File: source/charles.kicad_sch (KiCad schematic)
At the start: 35 parts, among them J1 HRO-TYPE-C-31-M-13C, J2 Tag-Connect_Plug_of_nails_6pin, J3 Solder Battery, J4 JST ACH, Q1 AO3401A, Q2 Q_NMOS_DGS, SW38 Reset Switch, SW39 Soft Off, U1 MS88SF3, U2 USBLC6-2P6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

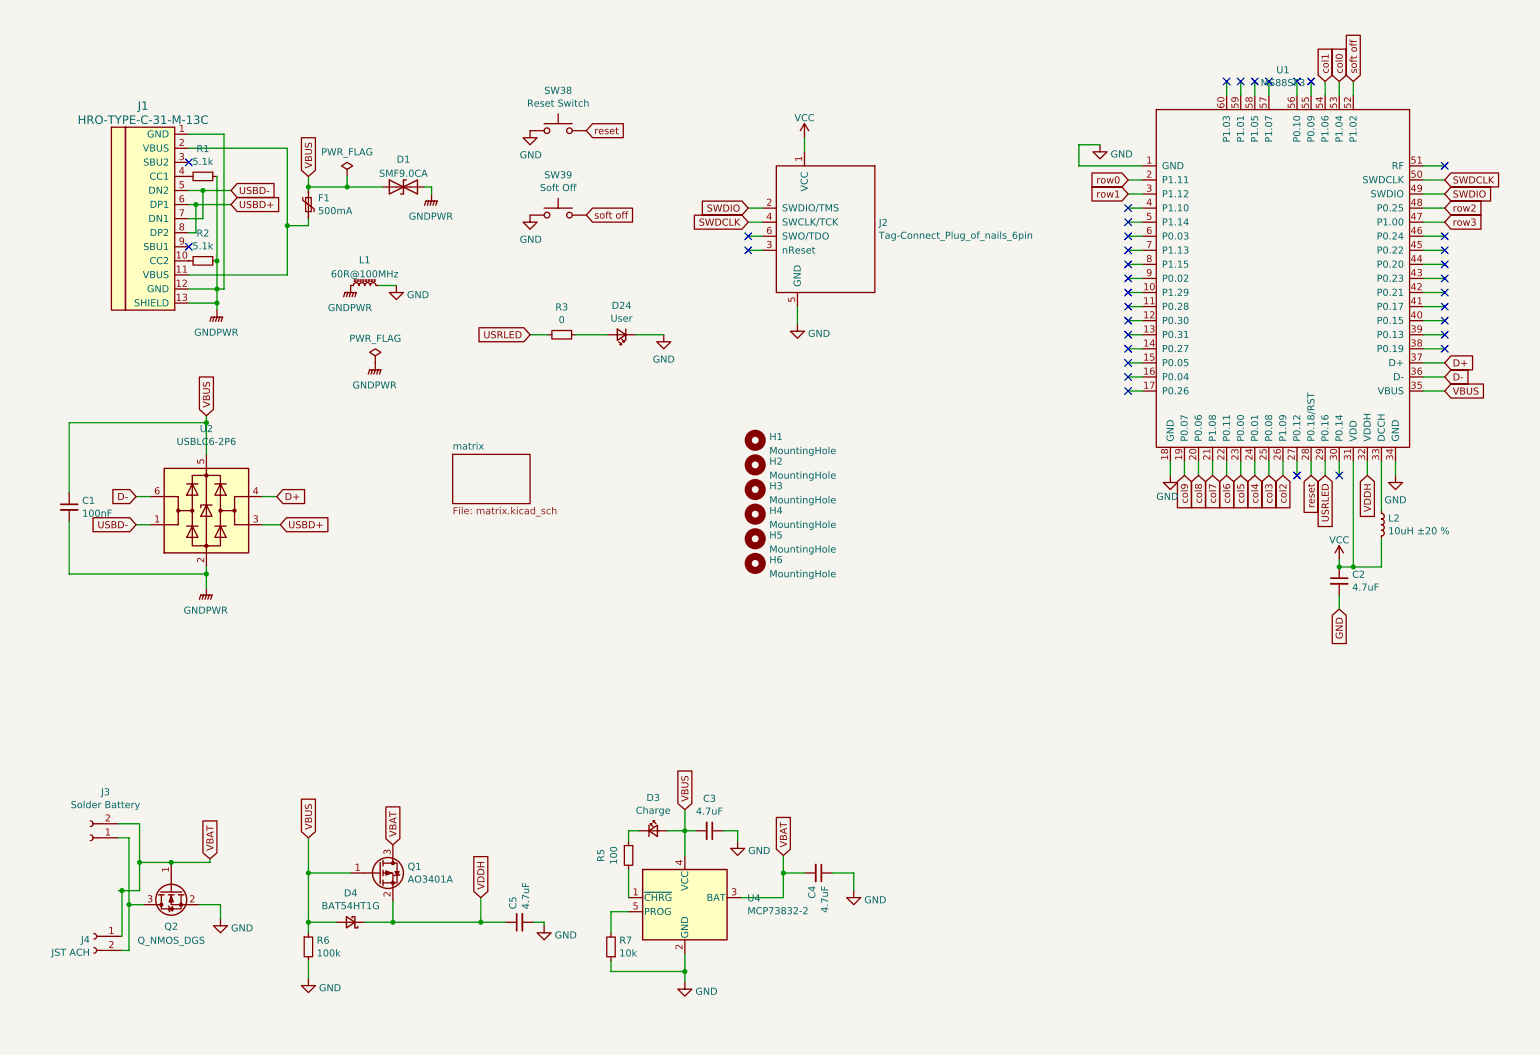
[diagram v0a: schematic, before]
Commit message: added non-jtag flash interface, zmk/osh silk, rearranging tracks
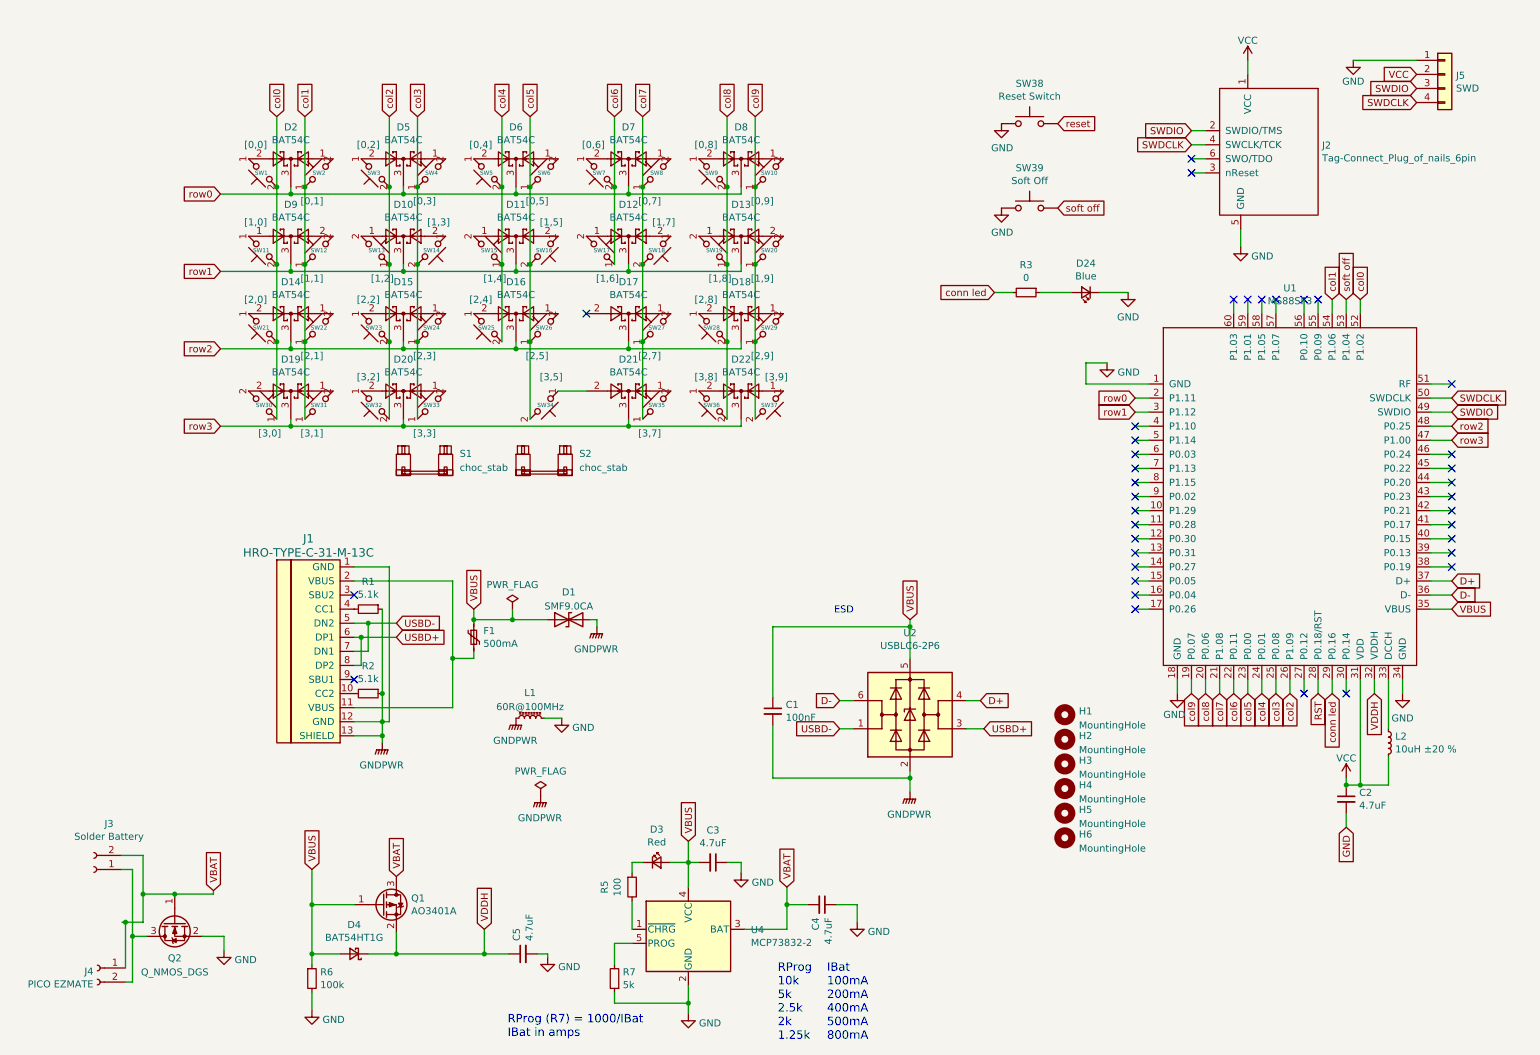
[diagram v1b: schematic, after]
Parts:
- added D10, D11, D12, D13, D14, D15, D16, D17, D18, D19, D2, D20, D21, D22, D5, D6, D7, D8, D9: BAT54C, Package_TO_SOT_SMD:SOT-23, symbol Diode:BAT54C
- added J5: SWD, Connector_PinHeader_2.54mm:PinHeader_1x04_P2.54mm_Vertical, symbol Connector_Generic:Conn_01x04
- added S1, S2: choc_stab, PCM_marbastlib-xp-choc:STAB_choc_2u, symbol PCM_marbastlib-choc:choc_stab
- added SW1: [0,0], chaz:choc-1u-millmax, symbol Switch:SW_Push_45deg
- added SW10: [0,9], chaz:choc-1u-millmax, symbol Switch:SW_Push_45deg
- added SW11: [1,0], chaz:choc-1u-millmax, symbol Switch:SW_Push_45deg
- added SW12: [1,1], chaz:choc-1u-millmax, symbol Switch:SW_Push_45deg
- added SW13: [1,2], chaz:choc-1u-millmax, symbol Switch:SW_Push_45deg
- added SW14: [1,3], chaz:choc-1u-millmax, symbol Switch:SW_Push_45deg
- added SW15: [1,4], chaz:choc-1u-millmax, symbol Switch:SW_Push_45deg
- added SW16: [1,5], chaz:choc-1u-millmax, symbol Switch:SW_Push_45deg
- added SW17: [1,6], chaz:choc-1u-millmax, symbol Switch:SW_Push_45deg
- added SW18: [1,7], chaz:choc-1u-millmax, symbol Switch:SW_Push_45deg
- added SW19: [1,8], chaz:choc-1u-millmax, symbol Switch:SW_Push_45deg
- added SW2: [0,1], chaz:choc-1u-millmax, symbol Switch:SW_Push_45deg
- added SW20: [1,9], chaz:choc-1u-millmax, symbol Switch:SW_Push_45deg
- added SW21: [2,0], chaz:choc-1u-millmax, symbol Switch:SW_Push_45deg
- added SW22: [2,1], chaz:choc-1u-millmax, symbol Switch:SW_Push_45deg
- added SW23: [2,2], chaz:choc-1u-millmax, symbol Switch:SW_Push_45deg
- added SW24: [2,3], chaz:choc-1u-millmax, symbol Switch:SW_Push_45deg
- added SW25: [2,4], chaz:choc-1u-millmax, symbol Switch:SW_Push_45deg
- added SW26: [2,5], chaz:choc-1u-millmax, symbol Switch:SW_Push_45deg
- added SW27: [2,7], chaz:choc-1u-millmax, symbol Switch:SW_Push_45deg
- added SW28: [2,8], chaz:choc-1u-millmax, symbol Switch:SW_Push_45deg
- added SW29: [2,9], chaz:choc-1u-millmax, symbol Switch:SW_Push_45deg
- added SW3: [0,2], chaz:choc-1u-millmax, symbol Switch:SW_Push_45deg
- added SW30: [3,0], chaz:choc-1u-millmax, symbol Switch:SW_Push_45deg
- added SW31: [3,1], chaz:choc-1u-millmax, symbol Switch:SW_Push_45deg
- added SW32: [3,2], chaz:choc-1u-millmax, symbol Switch:SW_Push_45deg
- added SW33: [3,3], chaz:choc-1u-millmax, symbol Switch:SW_Push_45deg
- added SW34: [3,5], chaz:choc-1u-millmax, symbol Switch:SW_Push_45deg
- added SW35: [3,7], chaz:choc-1u-millmax, symbol Switch:SW_Push_45deg
- added SW36: [3,8], chaz:choc-1u-millmax, symbol Switch:SW_Push_45deg
- added SW37: [3,9], chaz:choc-1u-millmax, symbol Switch:SW_Push_45deg
- added SW4: [0,3], chaz:choc-1u-millmax, symbol Switch:SW_Push_45deg
- added SW5: [0,4], chaz:choc-1u-millmax, symbol Switch:SW_Push_45deg
- added SW6: [0,5], chaz:choc-1u-millmax, symbol Switch:SW_Push_45deg
- added SW7: [0,6], chaz:choc-1u-millmax, symbol Switch:SW_Push_45deg
- added SW8: [0,7], chaz:choc-1u-millmax, symbol Switch:SW_Push_45deg
- added SW9: [0,8], chaz:choc-1u-millmax, symbol Switch:SW_Push_45deg
- D24: value User -> Blue
- D3: value Charge -> Red
- J4: value JST ACH -> PICO EZMATE; footprint Connector_JST:JST_ACH_BM02B-ACHSS-GAN-ETF_1x02-1MP_P1.20mm_Vertical -> PCM_marbastlib-various:Molex_Pico-EZmate_78171-0002_1x02-1MP_P1.20mm_Vertical
- R7: value 10k -> 5k
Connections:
- net GND: now also J5.1 (Pin_1)
- net SWDCLK: now also J5.4 (Pin_4)
- net SWDIO: now also J5.3 (Pin_3)
- net VCC: now also J5.2 (Pin_2)
- net col0: now also U1.52 (P1.02), SW1.2, SW11.2, SW21.2, SW30.1; no longer U1.53 (P1.04)
- net col1: now also SW12.1, SW2.1, SW22.1, SW31.1
- net col2: now also SW13.1, SW23.2, SW3.2, SW32.2
- net col3: now also SW14.2, SW24.1, SW33.1, SW4.1
- net col4: now also SW15.1, SW25.2, SW5.2
- net col5: now also SW16.2, SW26.1, SW34.2, SW6.1
- net col6: now also SW17.1, SW7.2
- net col7: now also SW18.2, SW27.1, SW35.1, SW8.1
- net col8: now also SW19.1, SW28.2, SW36.2, SW9.2
- net col9: now also SW10.1, SW20.1, SW29.1, SW37.2
- net reset: no longer U1.28 (P0.18/RST)
- net row0: now also D2.3, D5.3, D6.3, D7.3, D8.3
- net row1: now also D10.3, D11.3, D12.3, D13.3, D9.3
- net row2: now also D14.3, D15.3, D16.3, D17.3, D18.3
- net row3: now also D19.3, D20.3, D21.3, D22.3
- net soft off: now also U1.53 (P1.04); no longer U1.52 (P1.02)
- net USRLED renamed conn led
- new net: D12.1, SW17.2
- new net: D13.2, SW20.2
- new net: D17.1, SW27.2
- new net: D16.2, SW25.1
- new net: D10.1, SW13.2
- new net: D10.2, SW14.1
- new net: D6.2, SW5.1
- new net: D6.1, SW6.2
- new net: D9.1, SW11.1
- new net: D9.2, SW12.2
- new net: D7.1, SW8.2
- new net: D7.2, SW7.1
- new net: D19.1, SW31.2
- new net: D19.2, SW30.2
- new net: D14.1, SW22.2
- new net: D13.1, SW19.2
- new net: D5.1, SW4.2
- new net: D5.2, SW3.1
- new net: D16.1, SW26.2
- new net: D12.2, SW18.1
- new net: D2.2, SW1.1
- new net: D18.1, SW29.2
- new net: D8.2, SW9.1
- new net: D15.2, SW23.1
- new net: D22.1, SW37.1
- new net: D22.2, SW36.1
- new net: D14.2, SW21.1
- new net: D18.2, SW28.1
- new net: D20.2, SW32.1
- new net: D11.1, SW15.2
- new net: D8.1, SW10.2
- new net: D2.1, SW2.2
- new net: D15.1, SW24.2
- new net: D20.1, SW33.2
- new net: D21.1, SW35.2
- new net: D21.2, SW34.1
- new net: D11.2, SW16.1
- new net RST: U1.28 (P0.18/RST)
- no-connect marks 36 -> 37
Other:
- removed sheet matrix
- note added: "ESD"
- note added: "IBat 100mA 200mA 400mA 500mA 800mA"
- note added: "RProg (R7) = 1000/IBat IBat in amps"
- note added: "RProg 10k 5k 2.5k 2k 1.25k"
- moved on the sheet: C1, C2, C3, C4, C5, D1, D24, D3, D4, F1, H1, H2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

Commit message: added logo, connected necessary gnds
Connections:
- net reset is gone; now on net RST: SW38.2
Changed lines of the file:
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@@
 		)
 	)
-	(global_label "reset"
+	(global_label "RST"
 		(shape input)
 		(at 201.93 30.48 0)

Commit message: added logo
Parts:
- R3: value 0 -> 220
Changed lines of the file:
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@@
 			)
 		)
-		(property "Value" "0"
+		(property "Value" "220"
 			(at 196.215 58.293 90)
 			(effects
